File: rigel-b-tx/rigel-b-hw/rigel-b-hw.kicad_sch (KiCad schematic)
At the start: 49 parts, among them IC1 BALFHB-WL-02D3, J1 Conn_01x03_Pin, J2 436500200, J3 Conn_01x03_Pin, U1 STM32WLE5C8Ux, U2 TPS629206DRLR, U3 CH340X, U4 TYPE-C_16PIN_2MD(073), U5 X1G004131004200, U6 KH-SMA-K513-G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

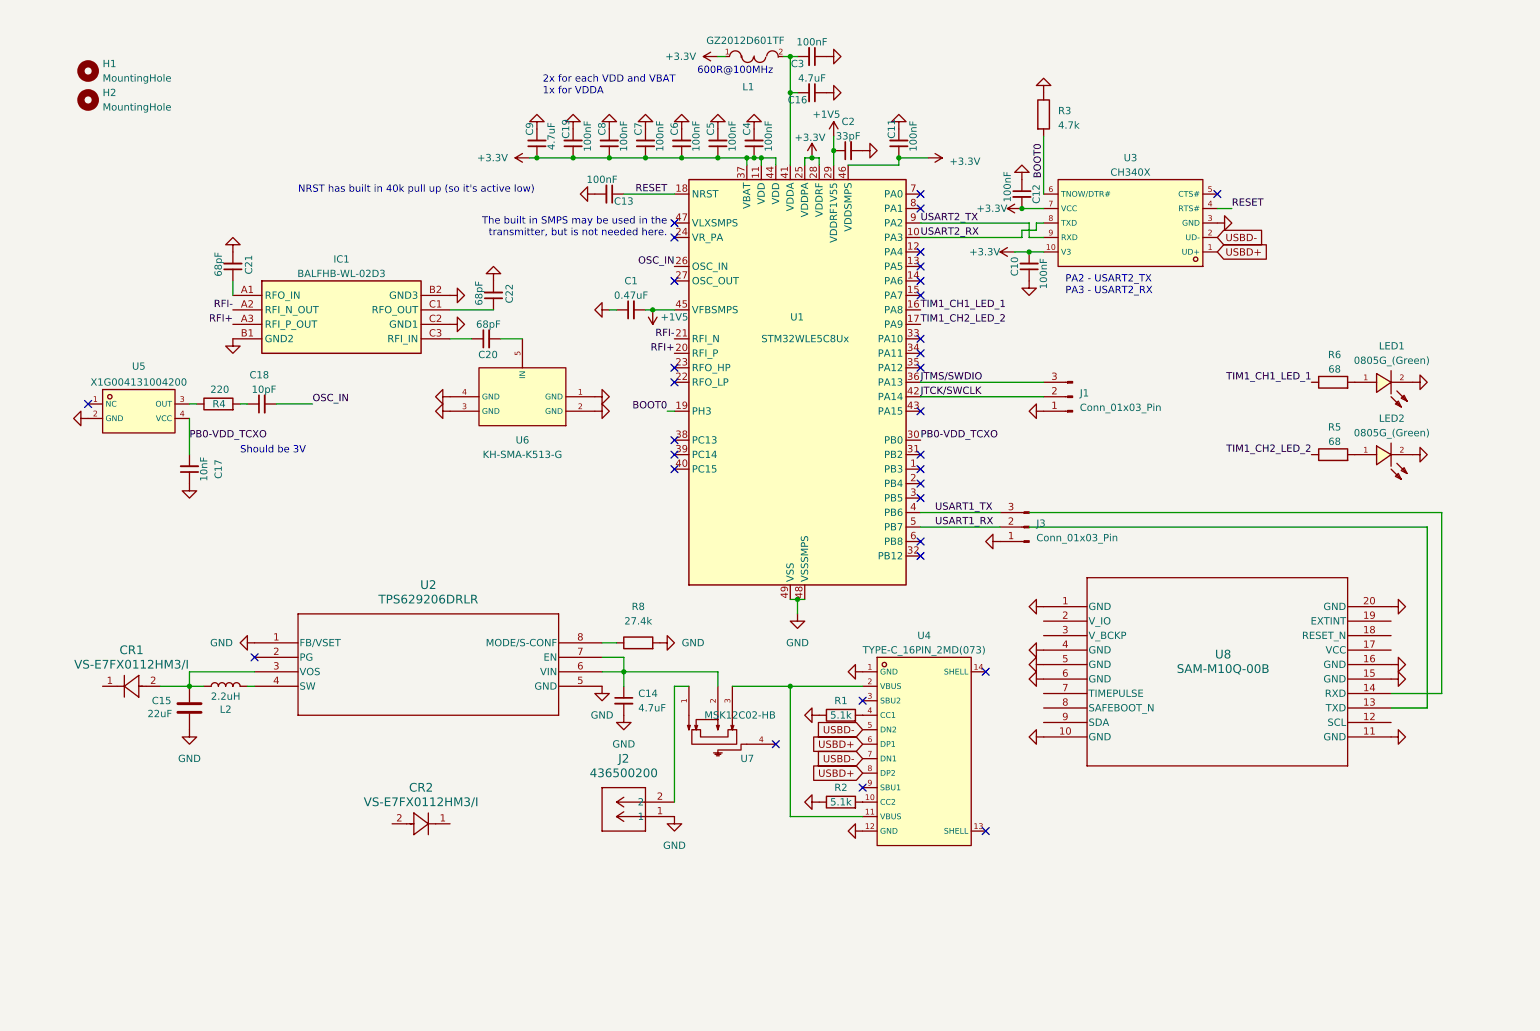
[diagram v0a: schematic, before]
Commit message: RF Switch
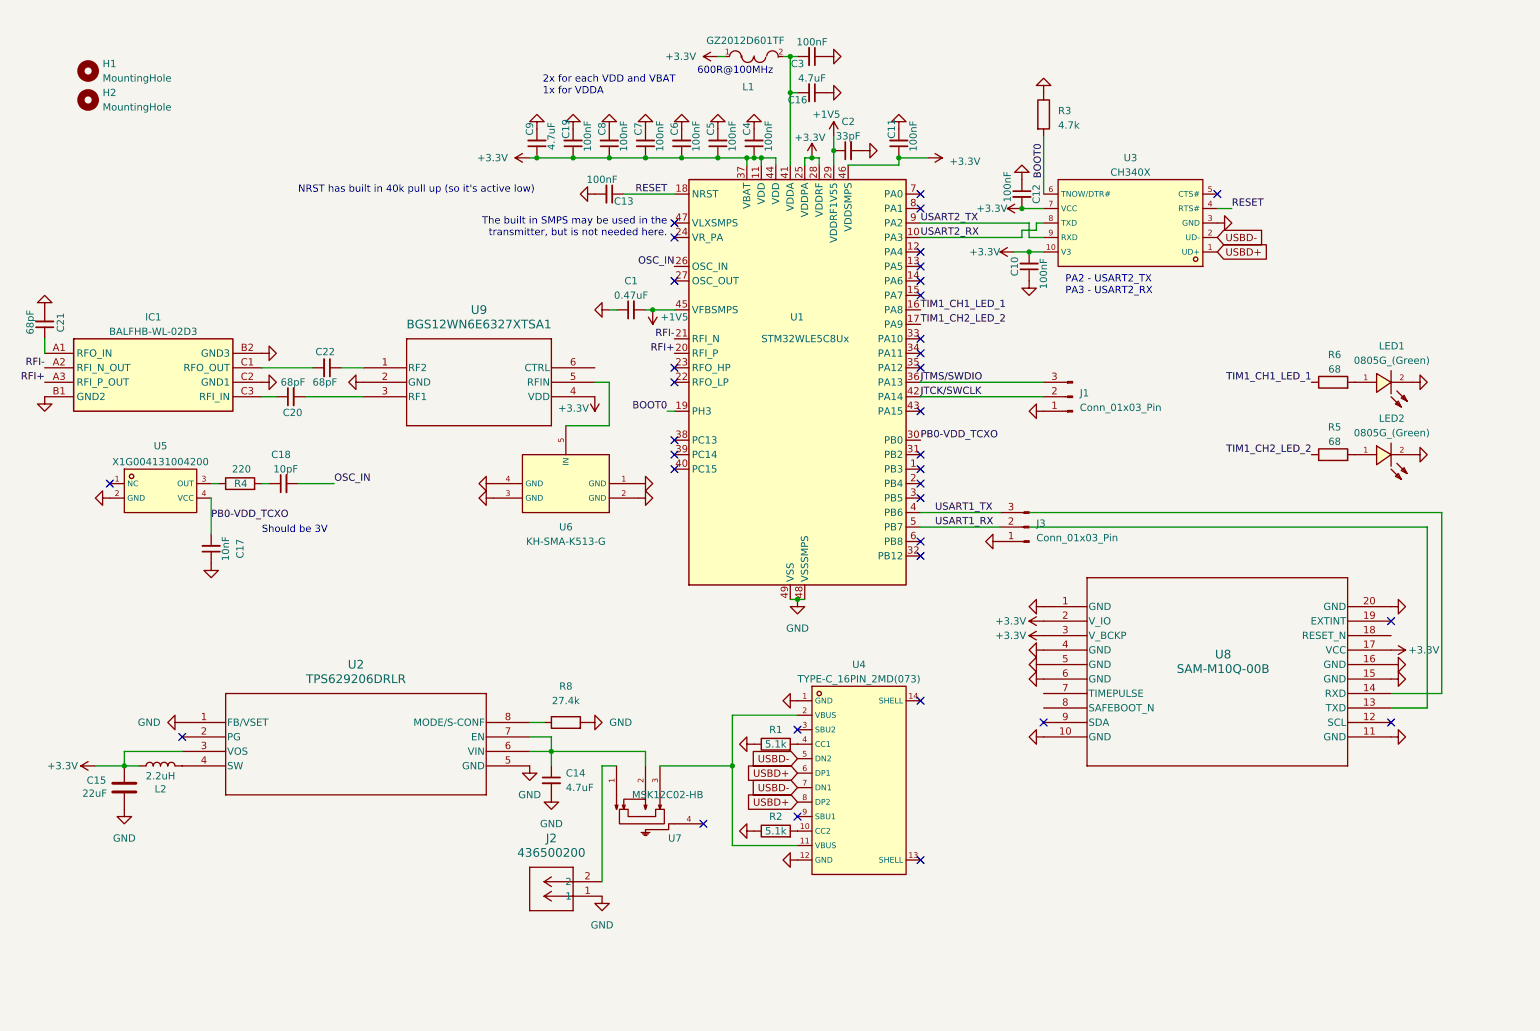
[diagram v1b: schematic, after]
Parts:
- removed CR1, CR2: VS-E7FX0112HM3/I, CR_SMF_DO-219AB_VIS, symbol 2024-11-05_21-21-38:VS-E7FX0112HM3_I
- added U9: BGS12WN6E6327XTSA1, PG-TSNP-6-10_INF, symbol 2024-11-10_21-59-30:BGS12WN6E6327XTSA1
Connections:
- net +3.3V: now also C15.2, L2.1, U2.3 (VOS), U8.17 (VCC), U8.2 (V_IO), U8.3 (V_BCKP), U9.4 (VDD)
- net GND: now also U9.2 (GND); no longer C22.2
- net at C20.2: now also U9.3 (RF1); no longer U6.5 (IN)
- net at C22.1: now also U9.1 (RF2); no longer IC1.C1 (RFO_OUT)
- new net: U6.5 (IN), U9.5 (RFIN)
- new net: C22.2, IC1.C1 (RFO_OUT)
- no-connect marks 32 -> 35
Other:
- moved on the sheet: C14, C15, C17, C18, C20, C21, C22, IC1, J2, L2, R1, R2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

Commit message: Connection
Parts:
- added C23, C24, C25, C26: 100nF, symbol Device:C
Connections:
- net +3.3V: now also C23.2, C24.2, C25.2, C26.2
- net GND: now also C23.1, C24.1, C25.1, C26.1
- net at U9.6 (CTRL): now also U1.38 (PC13)
- no-connect marks 35 -> 36
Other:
- moved on the sheet: U6

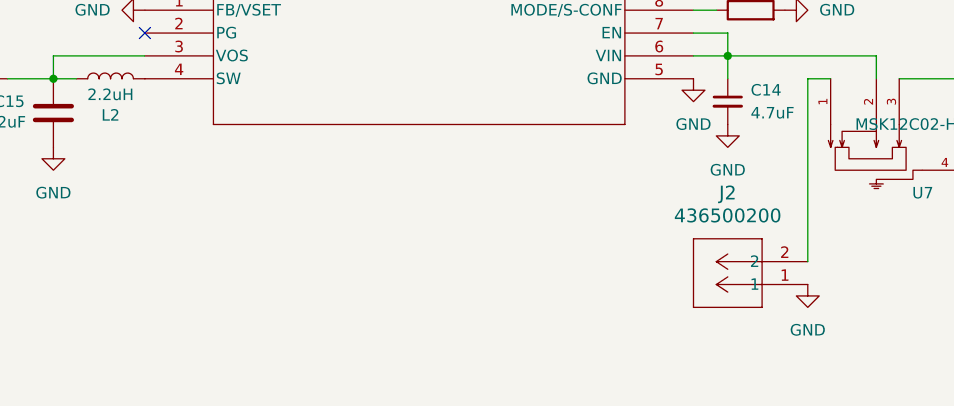
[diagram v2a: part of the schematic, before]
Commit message: Board to Board & Battery Connectors
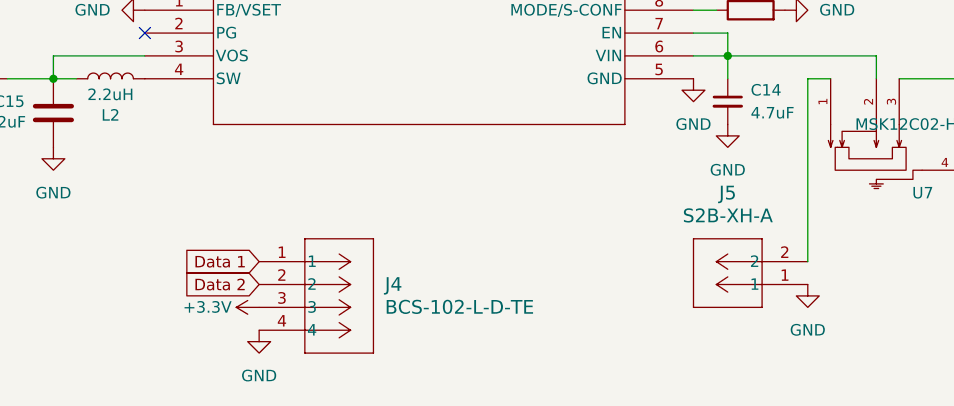
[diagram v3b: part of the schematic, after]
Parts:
- removed J2: 436500200, CON_436500200_MOL, symbol 2024-11-03_22-45-00:436500200
- added J4: BCS-102-L-D-TE, CON4_2X2_TU_BCS_SAI, symbol 2024-11-12_20-08-53:BCS-102-L-D-TE
- added J5: S2B-XH-A, CONN_S2B-XH-A_JST, symbol 2024-11-12_20-50-55:S2B-XH-A
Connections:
- net +3.3V: now also J4.3
- net GND: now also J4.4, J5.1
- net at U7.1: now also J5.2
- new net Data 1: J4.1
- new net Data 2: J4.2

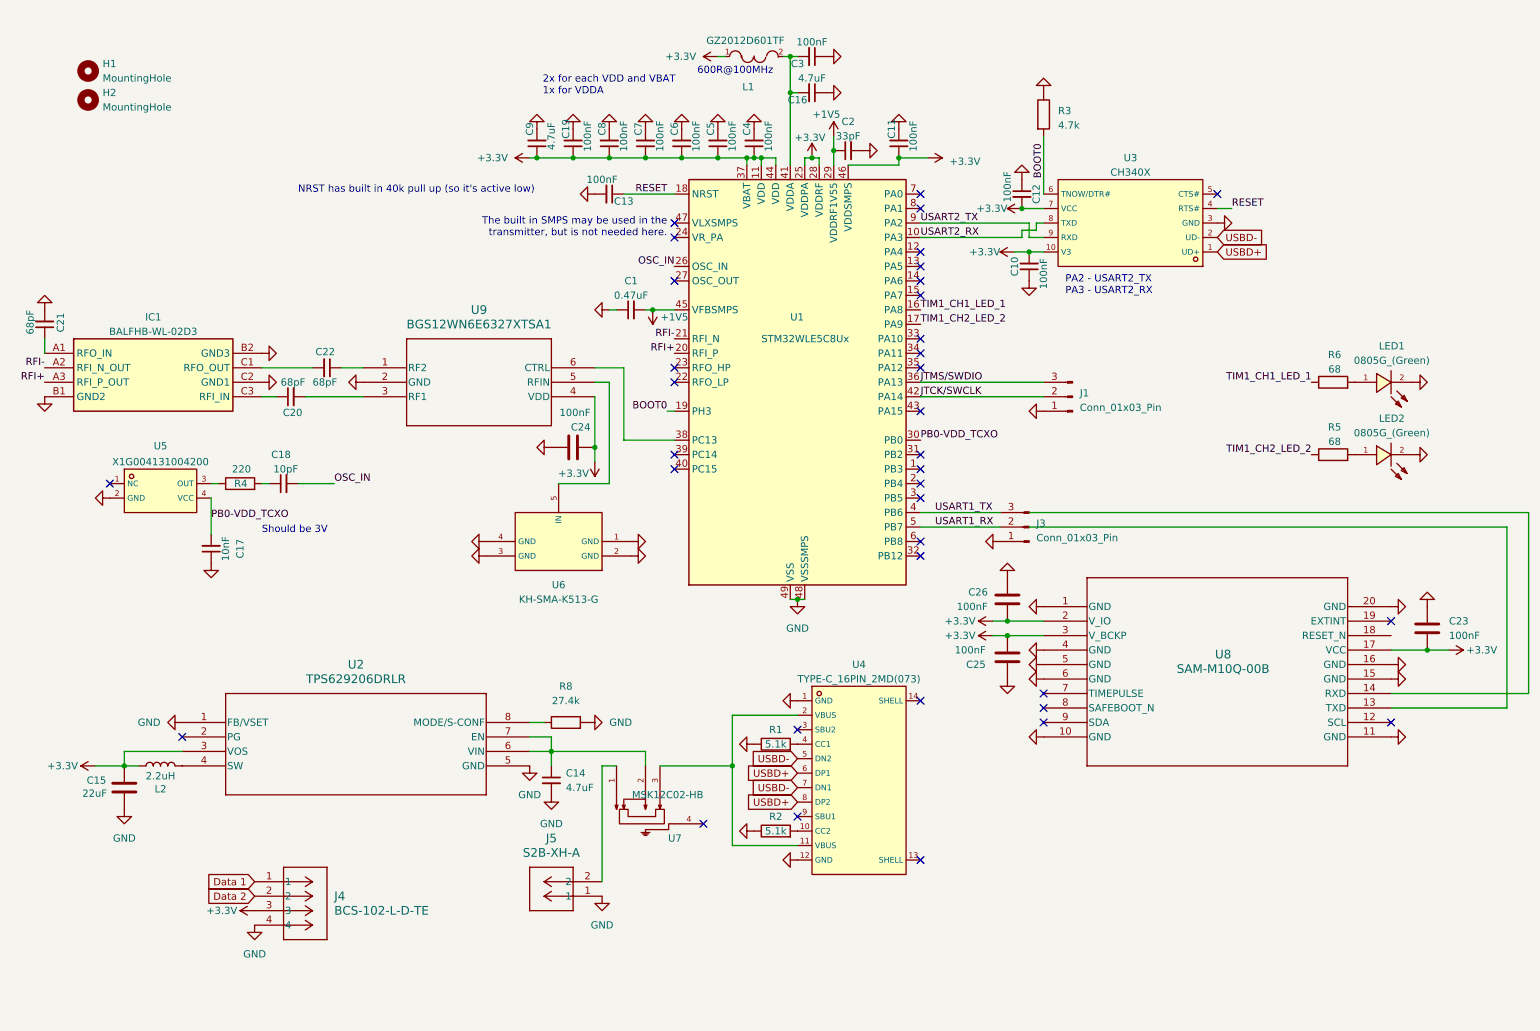
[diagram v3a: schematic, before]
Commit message: Update connections based off example schematic
https://www.st.com/resource/en/schematic_pack/mb1848-hp-schematic.pdf
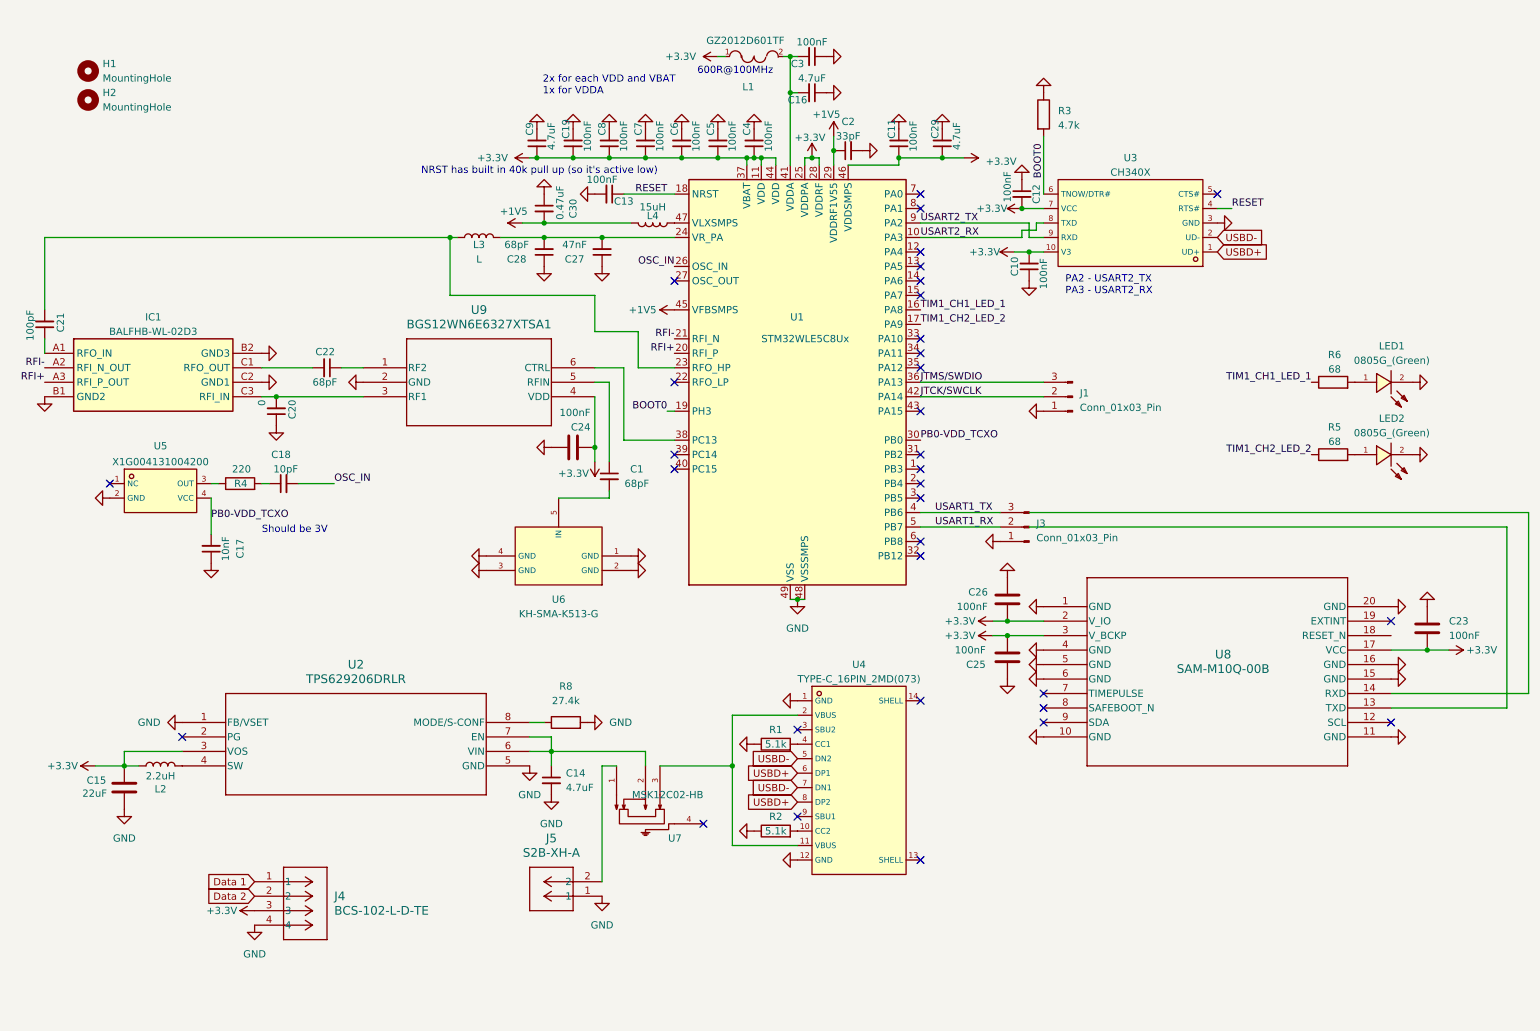
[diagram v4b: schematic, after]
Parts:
- added C27: 47nF, Capacitor_SMD:C_0603_1608Metric, symbol Device:C_Small
- added C28: 68pF, Capacitor_SMD:C_0603_1608Metric, symbol Device:C_Small
- added C29: 4.7uF, Capacitor_SMD:C_0402_1005Metric, symbol Device:C_Small
- added C30: 0.47uF, Capacitor_SMD:C_0603_1608Metric, symbol Device:C_Small
- added L3: L, symbol Device:L
- added L4: 15uH, symbol Device:L
- C1: value 0.47uF -> 68pF
- C20: value 68pF -> 0
- C21: value 68pF -> 100pF
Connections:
- net +1V5: now also C30.2, L4.2; no longer C1.2
- net +3.3V: now also C29.1
- net GND: now also C20.1, C27.1, C28.1, C29.2, C30.1; no longer C1.1, C21.2
- net at IC1.C3 (RFI_IN): now also C20.2, U9.3 (RF1); no longer C20.1
- net at U9.5 (RFIN): now also C1.1; no longer U6.5 (IN)
- net at U1.23 (RFO_HP): now also C21.2, L3.1
- net at U1.24 (VR_PA): now also C27.2, C28.2, L3.2
- net at U1.47 (VLXSMPS): now also L4.1
- new net: C1.2, U6.5 (IN)
- no-connect marks 36 -> 33
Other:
- note removed: "The built in SMPS may be used in the transmitter, but is not needed here."
- moved on the sheet: C20, U6

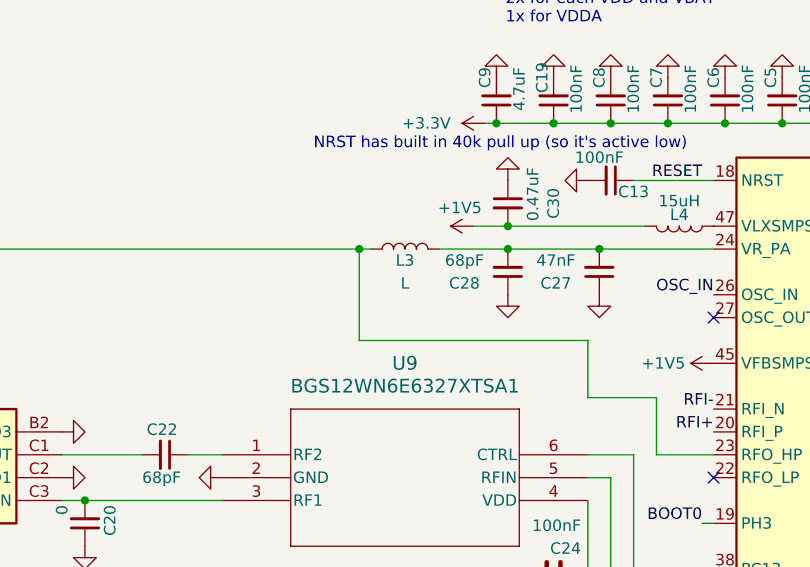
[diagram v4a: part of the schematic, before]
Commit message: Footprints. Done with Schematic
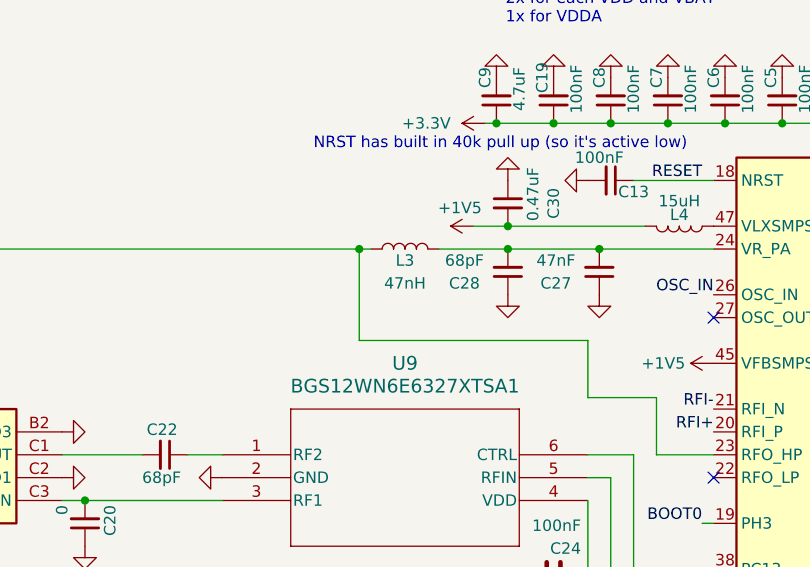
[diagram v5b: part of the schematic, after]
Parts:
- C23, C24, C25, C26: footprint (none) -> Capacitor_SMD:C_0402_1005Metric
- J4: footprint CON4_2X2_TU_BCS_SAI -> jlc:CON4_2X2_TU_BCS_SAI
- J5: footprint CONN_S2B-XH-A_JST -> jlc:CONN_S2B-XH-A_JST
- L3: value L -> 47nH; footprint (none) -> Inductor_SMD:L_0603_1608Metric
- L4: footprint (none) -> Inductor_SMD:L_0603_1608Metric
- U9: footprint PG-TSNP-6-10_INF -> jlc:PG-TSNP-6-10_INF
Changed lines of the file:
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@@
 			)
 		)
-		(property "Value" "L"
+		(property "Value" "47nH"
 			(at 93.98 63.5 90)
 			(effects
@@
 			)
 		)
-		(property "Footprint" ""
+		(property "Footprint" "Inductor_SMD:L_0603_1608Metric"
 			(at 93.98 59.69 0)
 			(effects
@@
 			)
 		)
-		(property "Footprint" ""
+		(property "Footprint" "Capacitor_SMD:C_0402_1005Metric"
 			(at 114.3 95.5548 0)
 			(effects
@@
 			)
 		)
-		(property "Footprint" "PG-TSNP-6-10_INF"
+		(property "Footprint" "jlc:PG-TSNP-6-10_INF"
 			(at 73.66 82.55 0)
 			(effects
@@
 			)
 		)
-		(property "Footprint" "CONN_S2B-XH-A_JST"
+		(property "Footprint" "jlc:CONN_S2B-XH-A_JST"
 			(at 115.57 175.26 0)
 			(effects
@@
 			)
 		)
-		(property "Footprint" "CON4_2X2_TU_BCS_SAI"
+		(property "Footprint" "jlc:CON4_2X2_TU_BCS_SAI"
 			(at 54.61 172.72 0)
 			(effects
@@
 			)
 		)
-		(property "Footprint" ""
+		(property "Footprint" "Capacitor_SMD:C_0402_1005Metric"
 			(at 261.3152 132.08 0)
 			(effects
@@
 			)
 		)
-		(property "Footprint" ""
+		(property "Footprint" "Capacitor_SMD:C_0402_1005Metric"
 			(at 185.7248 129.54 0)
 			(effects
@@
 			)
 		)
-		(property "Footprint" ""
+		(property "Footprint" "Inductor_SMD:L_0603_1608Metric"
 			(at 124.46 57.15 0)
 			(effects
@@
 			)
 		)
-		(property "Footprint" ""
+		(property "Footprint" "Capacitor_SMD:C_0402_1005Metric"
 			(at 187.6552 127 0)
 			(effects
